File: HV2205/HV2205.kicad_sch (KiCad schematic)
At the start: 64 parts, among them J1 OUTPUT, J2 OUTPUT, J3 OUTPUT, J4 OUTPUT TO NEXT STAGE, J5 OUTPUT, J6 INPUT FROM PREVIOUS STAGE, J7 POWER INPUT, U1 NJM4580

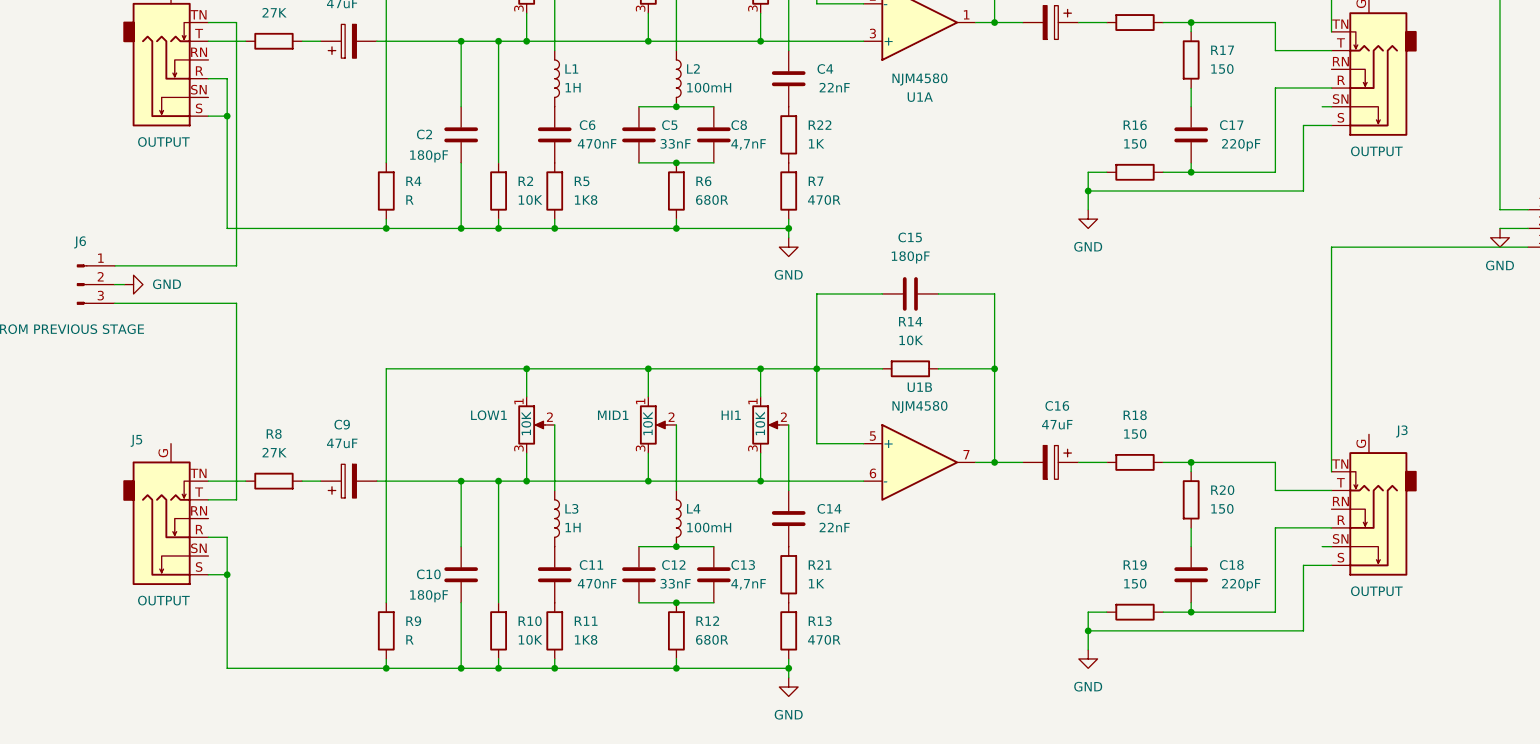
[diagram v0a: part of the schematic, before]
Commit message: HV1403 op_amp included to the archive
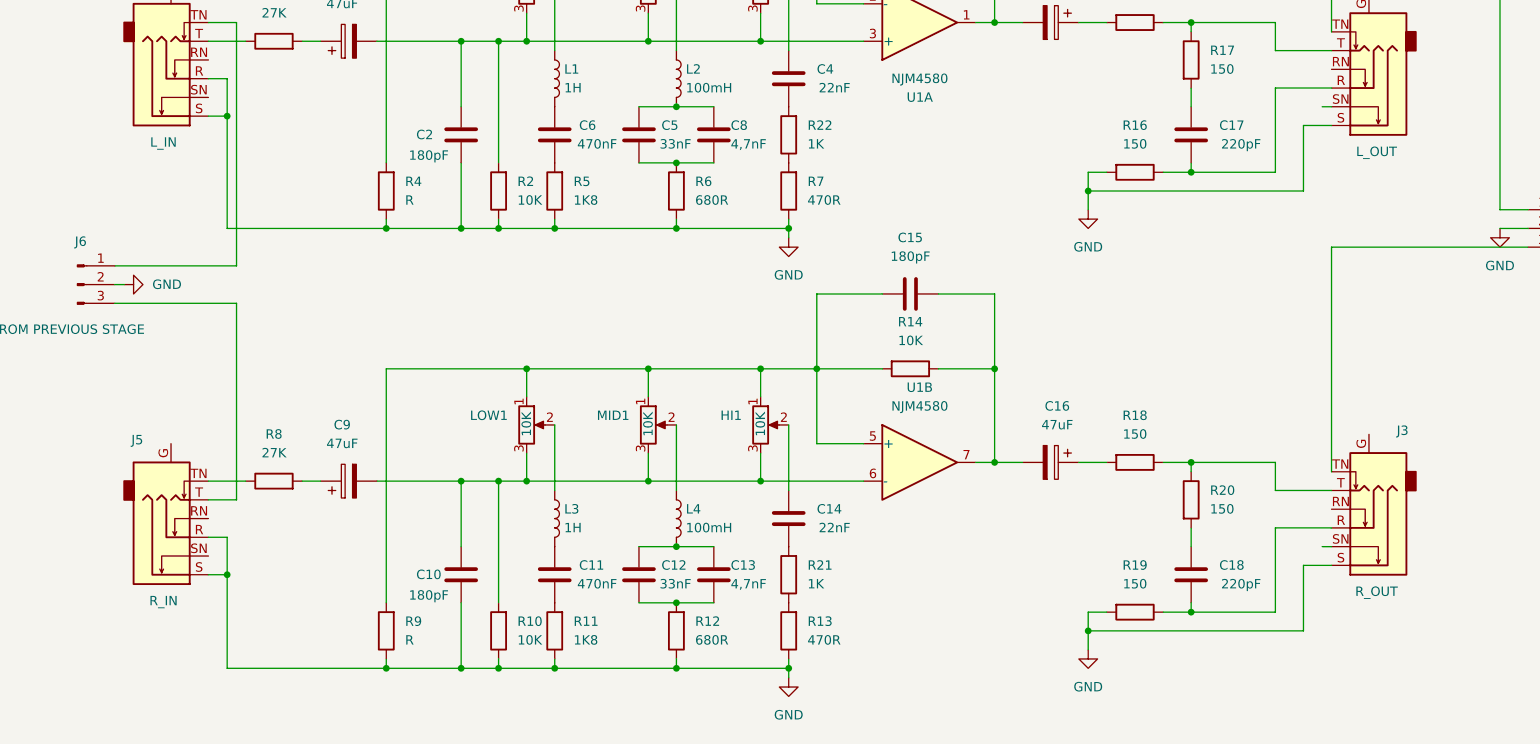
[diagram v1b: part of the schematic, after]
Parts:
- J1: value OUTPUT -> L_OUT
- J2: value OUTPUT -> L_IN
- J3: value OUTPUT -> R_OUT
- J5: value OUTPUT -> R_IN
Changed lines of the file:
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@@
 			)
 		)
-		(property "Value" "OUTPUT"
+		(property "Value" "L_IN"
 			(at 57.404 79.756 0)
 			(effects
@@
 			)
 		)
-		(property "Value" "OUTPUT"
+		(property "Value" "R_IN"
 			(at 57.404 141.986 0)
 			(effects
@@
 			)
 		)
-		(property "Value" "OUTPUT"
+		(property "Value" "L_OUT"
 			(at 221.996 81.026 0)
 			(effects
@@
 			)
 		)
-		(property "Value" "OUTPUT"
+		(property "Value" "R_OUT"
 			(at 221.996 140.716 0)
 			(effects
